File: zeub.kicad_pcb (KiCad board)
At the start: 2 copper layers, 177.8 x 60 mm, 377 parts, among them J1 debug-port, J2 OLED-128x32, J3 USB_C_Receptacle_USB2.0, J4 Barrel_Jack_Switch, J5 Conn_01x03, J6 Conn_01x03, Q1 AO3401A, Q2 AO3401A, Q3 AO3401A, Q4 AO3401A, Q5 AO3401A, SW1 SKRHA, SW2 RotaryEncoder_Switch, SW3 SW_Push, U1 IS31FL3729, U10 LTC4054ES5-4.2, U11 TMP117, U12 CMM4030D, U2 IS31FL3729, U3 IS31FL3729, U4 IS31FL3729, U5 holyiot-18010-no-underside, U6 MT25QL128ABA1ESE, U7 TLV1117-50, U8 XC6206PxxxMR, U9 SRV05-4

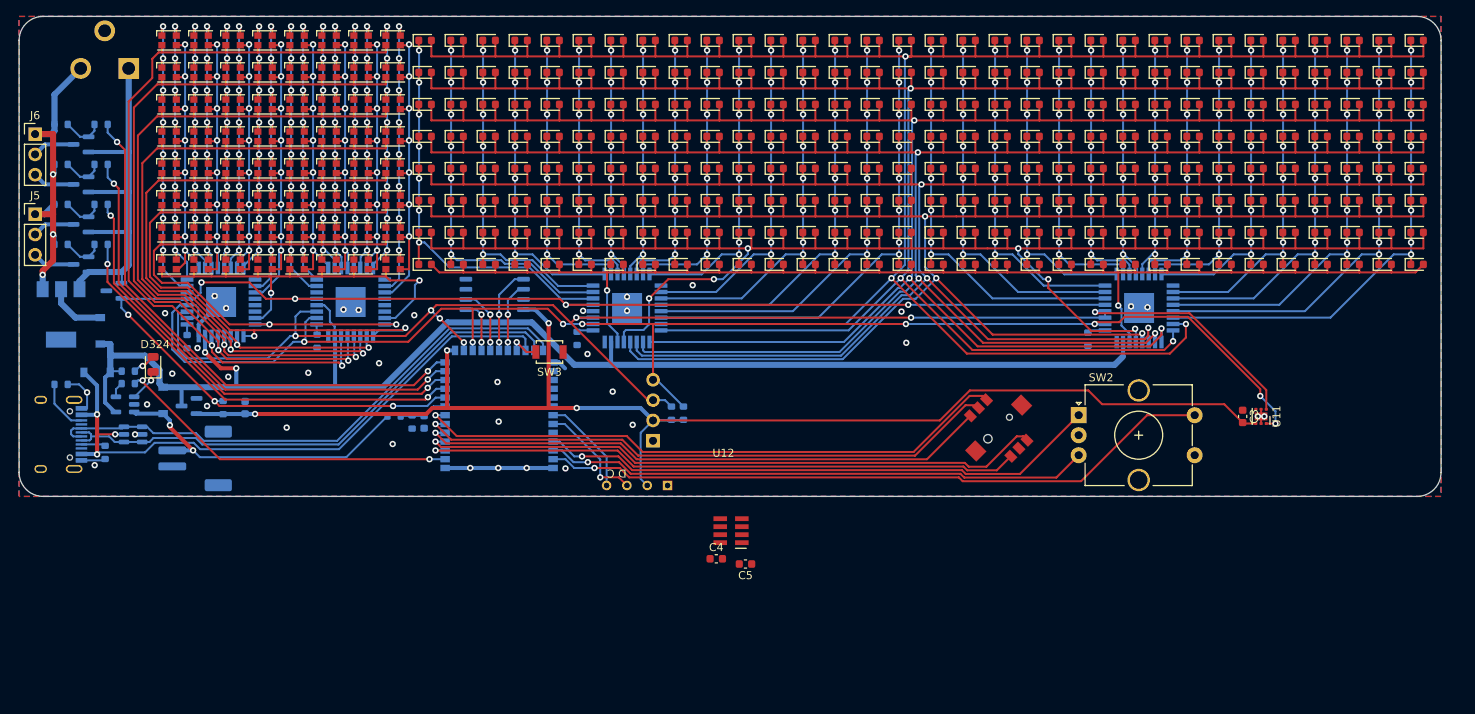
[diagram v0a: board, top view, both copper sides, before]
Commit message: Added audio stuff; rerouted for prep
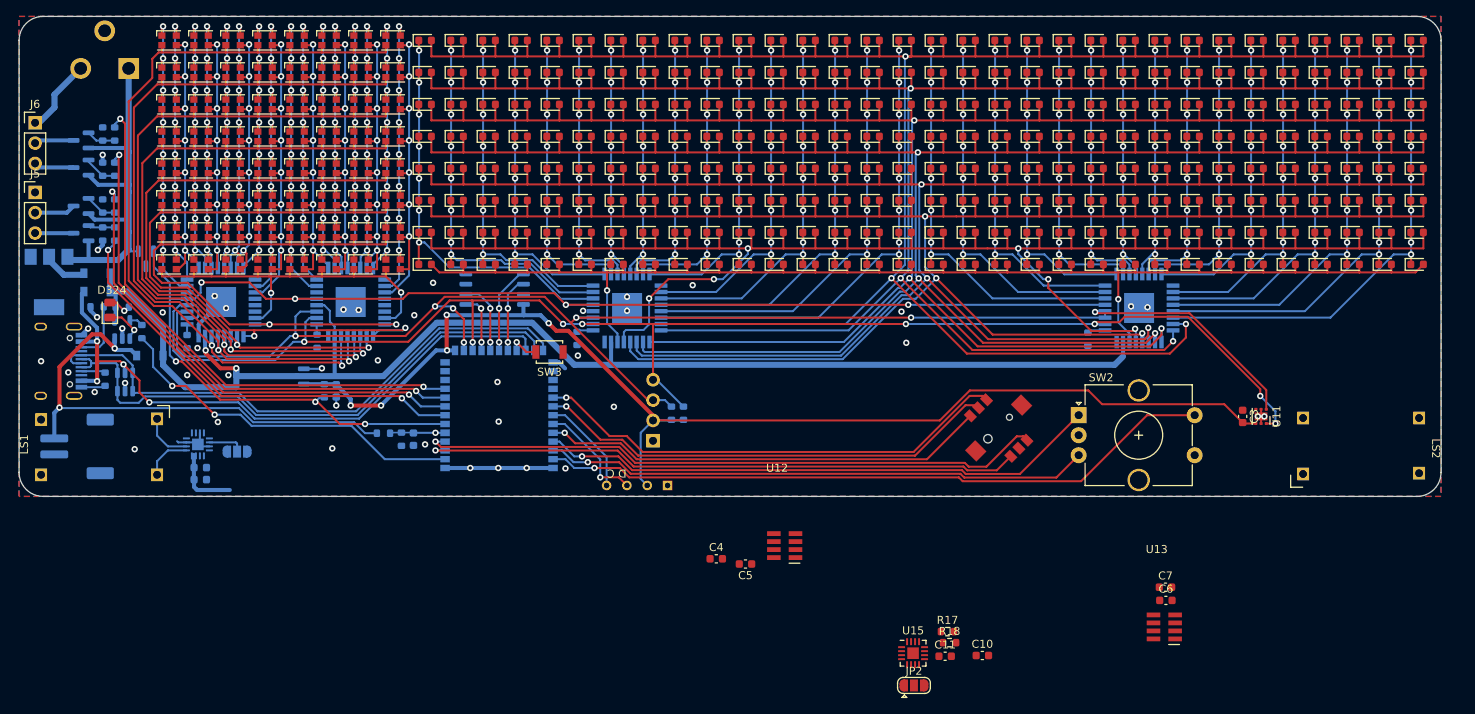
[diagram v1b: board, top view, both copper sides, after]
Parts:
- added C10: 0.1uF, Capacitor_SMD:C_0603_1608Metric, F.Cu at (101.7, 76.9)
- added C11: 10uF, Capacitor_SMD:C_0603_1608Metric, F.Cu at (97.0, 77.0)
- added C6: 10uF, Capacitor_SMD:C_0603_1608Metric, F.Cu at (124.6, 70.0)
- added C7: 0.1uF, Capacitor_SMD:C_0603_1608Metric, F.Cu at (124.5, 68.3)
- added C8: 0.1uF, Capacitor_SMD:C_0603_1608Metric, B.Cu at (3.90, 53.4)
- added C9: 10uF, Capacitor_SMD:C_0603_1608Metric, B.Cu at (3.90, 54.9)
- added JP1: SolderJumper_3_Open, Jumper:SolderJumper-3_P1.3mm_Open_RoundedPad1.0x1.5mm, B.Cu at (8.50, 51.4)
- added JP2: SolderJumper_3_Open, Jumper:SolderJumper-3_P1.3mm_Open_RoundedPad1.0x1.5mm, F.Cu at (93.1, 80.6)
- added LS1: Speaker, misc:CMS1609, F.Cu at (-8.75, 50.8)
- added LS2: Speaker, misc:CMS1609, F.Cu at (149.0, 50.8)
- added R17: 100k, Resistor_SMD:R_0603_1608Metric, F.Cu at (97.3, 73.9)
- added R18: 100k, Resistor_SMD:R_0603_1608Metric, F.Cu at (97.6, 75.3)
- added U13: CMM4030D, ic:CMM4030D_hand_solder, F.Cu at (124.4, 73.3)
- added U14: MAX98357A, Package_DFN_QFN:QFN-16-1EP_3x3mm_P0.5mm_EP1.45x1.45mm, B.Cu at (3.60, 50.5)
- added U15: MAX98357A, Package_DFN_QFN:QFN-16-1EP_3x3mm_P0.5mm_EP1.45x1.45mm, F.Cu at (93.0, 76.6)
- moved BT1 14.8 mm to (-11.5, 50.8)
- moved U8 13.9 mm to (15.9, 42.0)
- moved R73 12.8 mm to (19.4, 43.8), turned to -90 degrees
- moved C2 11.6 mm to (20.9, 43.8), turned to 90 degrees
- moved R10 10.7 mm to (-9.00, 33.3), turned to 0 degrees
- moved D321 10.1 mm to (-9.00, 31.4)
- moved U10 9.37 mm to (-5.85, 36.1), turned to 90 degrees
- moved J3 9.15 mm to (-15.0, 40.1)
- moved R9 9.15 mm to (-8.00, 42.4)
- moved D324 8.68 mm to (-7.40, 33.7)
- moved R11 8.05 mm to (-5.85, 33.3)
- moved D323 7.21 mm to (-9.00, 29.1), turned to 180 degrees
- moved U12 6.96 mm to (77.0, 63.1)
- moved R12 6.72 mm to (-3.40, 36.4), turned to -90 degrees
- moved U9 6.63 mm to (-5.50, 42.7), turned to 90 degrees
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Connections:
- U12 pad 2: unconnected-(U12-Pad2) -> (no net)
- U12 pad 3: unconnected-(U12-Pad3) -> LRCLK
- U12 pad 5: unconnected-(U12-Pad5) -> GND
- U12 pad 6: unconnected-(U12-Pad6) -> BCLK
- U12 pad 7: unconnected-(U12-Pad7) -> SDIN
- U5 pad 10: PWMY1 -> PWMW0
- U5 pad 11: PWMW1 -> unconnected-(U5-Pad11)
- U5 pad 12: PWMY0 -> unconnected-(U5-Pad12)
- U5 pad 13: PWMW0 -> unconnected-(U5-Pad13)
- U5 pad 36: unconnected-(U5-Pad36) -> C
- U5 pad 39: unconnected-(U5-Pad39) -> E
- U5 pad 40: unconnected-(U5-Pad40) -> A
- U5 pad 5: C -> BAT_MEAS
- U5 pad 6: E -> HAS_12V
- U5 pad 7: A -> PWMY1
- U5 pad 8: BAT_MEAS -> PWMW1
- U5 pad 9: HAS_12V -> PWMY0
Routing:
- net +BATT: track 39.2 -> 63.9 mm
- net GND: track 73.0 -> 50.8 mm, vias 40 -> 44
- net C: track 71.7 -> 55.8 mm
- net E: track 73.5 -> 58.5 mm
- net A: track 75.1 -> 60.1 mm
- net +3V3: track 172.2 -> 161.0 mm, vias 4 -> 5
- net +5V: track 180.9 -> 171.1 mm
- net Net-(U14-Pad10): track 0.00 -> 6.32 mm
- net Net-(LS1-Pad2): track 0.00 -> 5.92 mm
- net Net-(JP1-Pad2): track 0.00 -> 4.53 mm
- net /led/RGB_C7: track 53.7 -> 49.6 mm
- net +12V: track 49.0 -> 52.6 mm
- net D-: track 66.8 -> 70.3 mm
- net D+: track 69.3 -> 71.7 mm
- net PWMW1: track 58.0 -> 60.4 mm
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
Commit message: fully routed
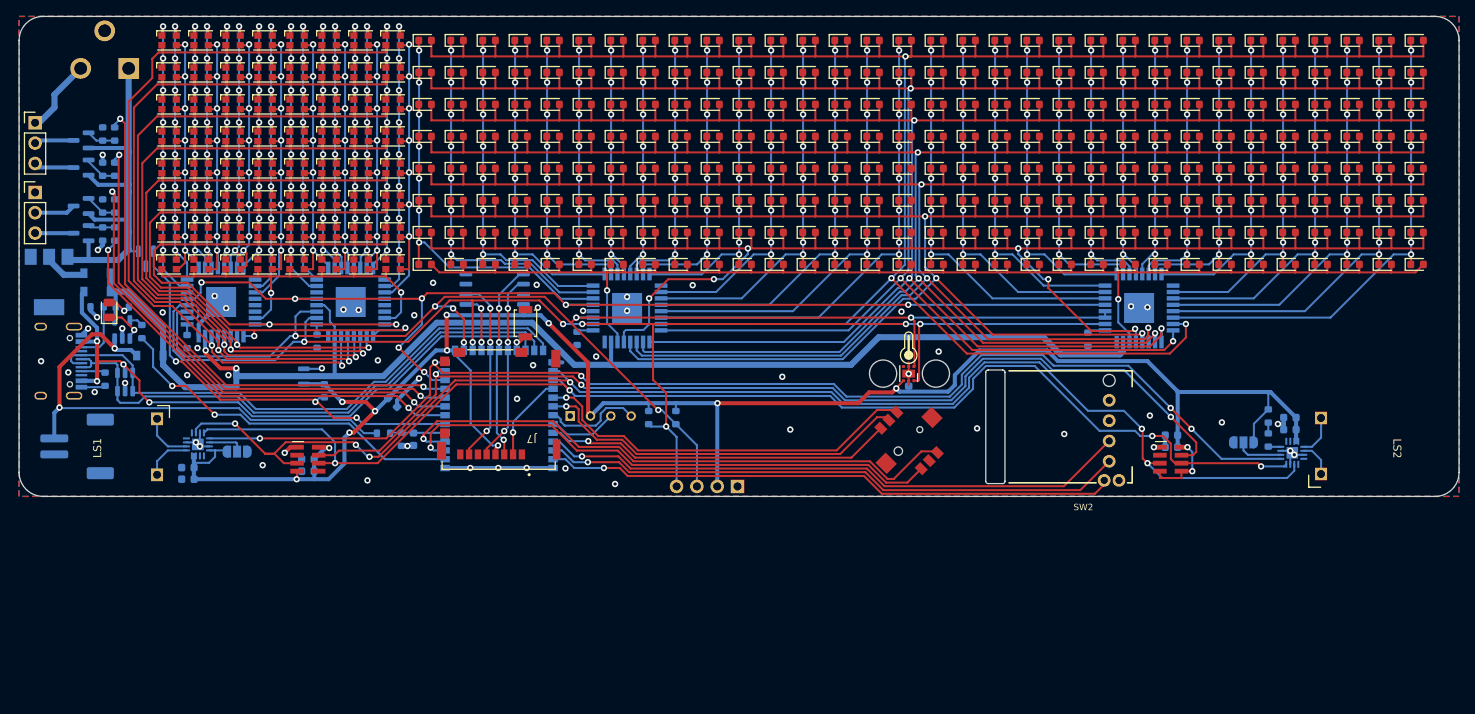
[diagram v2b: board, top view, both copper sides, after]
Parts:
- added J7: Micro_SD_Card_Det, misc:molex-503182-1852, F.Cu at (40.2, 45.3)
- C10, C11, C3, C4, C5, C6, C7, J1, JP2, R17, R18, U15: moved to B.Cu
- J2: footprint display:OLED-128x32-cutout -> display:OLED-128x64
- SW2: footprint Rotary_Encoder:RotaryEncoder_Alps_EC12E-Switch_Vertical_H20mm_CircularMountingHoles -> switch:EVQWGD001
- moved U12 60.6 mm to (17.4, 52.4), turned to 180 degrees
- moved C5 56.2 mm to (17.4, 52.4), turned to 0 degrees
- moved U15 53.6 mm to (140.4, 51.5)
- moved C11 52.4 mm to (140.1, 47.1)
- moved C4 52.2 mm to (17.4, 53.9)
- moved JP2 51.2 mm to (134.3, 50.2)
- moved R18 48.9 mm to (137.4, 47.0), turned to 90 degrees
- moved C10 47.7 mm to (140.1, 48.6)
- moved R17 46.7 mm to (137.4, 50.0), turned to 90 degrees
- moved U11 44.4 mm to (92.5, 41.6)
- moved C3 42.0 mm to (92.5, 42.5)
- moved U13 21.0 mm to (125.2, 52.4), turned to 180 degrees
- moved C6 20.7 mm to (125.3, 49.4)
- moved J2 17.6 mm to (67.2, 55.8), turned to 180 degrees
- moved C7 17.5 mm to (125.3, 50.9)
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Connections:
- LS2 pad 1: Net-(LS2-Pad1) -> Net-(U15-Pad10)
- LS2 pad 2: Net-(LS2-Pad2) -> Net-(U15-Pad9)
- SW2 pad S1: ENC_PUSH -> GND
- SW2 pad S2: GND -> ENC_PUSH
- U1 pad 29: HAS_12V -> ~{LED_SHDN}
- U15 pad 10: Net-(LS2-Pad2) -> Net-(U15-Pad10)
- U15 pad 9: Net-(LS2-Pad1) -> Net-(U15-Pad9)
- U2 pad 29: HAS_12V -> ~{LED_SHDN}
- U3 pad 29: HAS_12V -> ~{LED_SHDN}
- U4 pad 29: HAS_12V -> ~{LED_SHDN}
- U5 pad 11: unconnected-(U5-Pad11) -> ~{LED_SHDN}
- U5 pad 12: unconnected-(U5-Pad12) -> SDIN
- U5 pad 13: unconnected-(U5-Pad13) -> SDOUT
- U5 pad 34: ENC_B -> ENC_A
- U5 pad 35: ENC_A -> ENC_B
- U5 pad 41: unconnected-(U5-Pad41) -> SD_CS
- U5 pad 42: unconnected-(U5-Pad42) -> BCLK
- U5 pad 43: unconnected-(U5-Pad43) -> LRCLK
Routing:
- net LRCLK: track 0.00 -> 166.9 mm, vias 0 -> 6
- net BCLK: track 0.00 -> 158.0 mm, vias 0 -> 4
- net SDOUT: track 0.00 -> 151.3 mm, vias 0 -> 5
- net ~{LED_SHDN}: track 0.00 -> 139.0 mm, vias 0 -> 7
- net SDIN: track 0.00 -> 128.5 mm, vias 0 -> 3
- net HAS_12V: track 179.7 -> 53.4 mm, vias 7 -> 3
- net +3V3: track 161.0 -> 254.2 mm, vias 5 -> 13
- net MISO: track 9.24 -> 23.3 mm, vias 2 -> 3
- net ENC_PUSH: track 84.8 -> 71.2 mm
- net SCK: track 9.48 -> 22.9 mm, vias 2 -> 3
- net MOSI: track 11.1 -> 24.1 mm, vias 2 -> 3
- net GND: track 50.8 -> 63.5 mm, vias 44 -> 57
- net SCL: track 189.4 -> 176.9 mm
- net C: track 55.8 -> 43.8 mm
- net SDA: track 199.8 -> 188.2 mm, vias 8 -> 7
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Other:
- board size 177.8 x 60 mm -> 180 x 60 mm

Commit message: first version
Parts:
- added Q6: AO3401A, Package_TO_SOT_SMD:SOT-23, B.Cu at (-13.6, 10.7)
- added Q7: AO3401A, Package_TO_SOT_SMD:SOT-23, B.Cu at (-13.6, 14.6)
- added Q8: AO3401A, Package_TO_SOT_SMD:SOT-23, B.Cu at (-13.6, 19.4)
- added Q9: AO3401A, Package_TO_SOT_SMD:SOT-23, B.Cu at (-13.7, 23.7)
- added R19: 10k, Resistor_SMD:R_0603_1608Metric, B.Cu at (-10.9, 14.8)
- added R20: 10k, Resistor_SMD:R_0603_1608Metric, B.Cu at (-10.9, 19.6)
- added R21: 10k, Resistor_SMD:R_0603_1608Metric, B.Cu at (-11.0, 23.7)
- added R22: 100k, Resistor_SMD:R_0603_1608Metric, B.Cu at (-5.50, 10.5)
- added REF**: jlc-tooling-hole, misc:jlc-tooling-hole, F.Cu at (151.2, 50.8)
- added REF**: jlc-tooling-hole, misc:jlc-tooling-hole, F.Cu at (-14.6, 0.50)
- added REF**: jlc-tooling-hole, misc:jlc-tooling-hole, F.Cu at (-8.75, 50.8)
- D257, D258, D259, D260, D261, D262, D263, D264, D265, D266, D267, D268, D269, D270, D271, D272, D273, D274, D275, D276, D277, D278, D279, D280, D281, D282, D283, D284, D285, D286, D287, D288, D289, D290, D291, D292, D293, D294, D295, D296, D297, D298, D299, D300, D301, D302, D303, D304, D305, D306, D307, D308, D309, D310, D311, D312, D313, D314, D315, D316, D317, D318, D319, D320: value LED_RABG -> LED_BGRA
- Q1, Q2, Q3, Q4, Q5: value AO3401A -> AO3400A
- R5: value 100k -> 10k
- moved Q1 3.33 mm to (-8.20, 10.7)
- moved R7 3.18 mm to (-5.50, 19.2), turned to -90 degrees
- moved R3 3.18 mm to (-4.00, 19.2), turned to 90 degrees
- moved R6 3.13 mm to (-5.50, 14.7), turned to -90 degrees
- moved R2 3.13 mm to (-4.00, 14.7), turned to 90 degrees
- moved Q3 3.09 mm to (-8.20, 19.4)
- moved R1 3.05 mm to (-4.00, 10.5), turned to 90 degrees
- moved Q2 2.97 mm to (-8.20, 14.9)
- moved R5 2.82 mm to (-10.9, 10.6)
- moved R8 2.73 mm to (-5.60, 23.8)
- moved R4 2.73 mm to (-4.10, 23.8)
- moved Q4 2.71 mm to (-8.30, 23.9)
- moved C3 0.87 mm to (92.0, 41.7)
- moved U11 0.45 mm to (92.0, 41.6)
- moved D323 0.10 mm to (-9.00, 29.0)
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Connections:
- D257 pad 1: /led/RGB_R0 -> /led/RGB_B0
- D257 pad 2: /led/RGB_C0 -> /led/RGB_G0
- D257 pad 3: /led/RGB_B0 -> /led/RGB_R0
- D257 pad 4: /led/RGB_G0 -> /led/RGB_C0
- D258 pad 1: /led/RGB_R0 -> /led/RGB_B0
- D258 pad 2: /led/RGB_C1 -> /led/RGB_G0
- D258 pad 3: /led/RGB_B0 -> /led/RGB_R0
- D258 pad 4: /led/RGB_G0 -> /led/RGB_C1
- D259 pad 1: /led/RGB_R0 -> /led/RGB_B0
- D259 pad 2: /led/RGB_C2 -> /led/RGB_G0
- D259 pad 3: /led/RGB_B0 -> /led/RGB_R0
- D259 pad 4: /led/RGB_G0 -> /led/RGB_C2
- D260 pad 1: /led/RGB_R0 -> /led/RGB_B0
- D260 pad 2: /led/RGB_C3 -> /led/RGB_G0
- D260 pad 3: /led/RGB_B0 -> /led/RGB_R0
- D260 pad 4: /led/RGB_G0 -> /led/RGB_C3
- D261 pad 1: /led/RGB_R0 -> /led/RGB_B0
- D261 pad 2: /led/RGB_C4 -> /led/RGB_G0
- D261 pad 3: /led/RGB_B0 -> /led/RGB_R0
- D261 pad 4: /led/RGB_G0 -> /led/RGB_C4
- D262 pad 1: /led/RGB_R0 -> /led/RGB_B0
- D262 pad 2: /led/RGB_C5 -> /led/RGB_G0
- D262 pad 3: /led/RGB_B0 -> /led/RGB_R0
- D262 pad 4: /led/RGB_G0 -> /led/RGB_C5
- D263 pad 1: /led/RGB_R0 -> /led/RGB_B0
- D263 pad 2: /led/RGB_C6 -> /led/RGB_G0
- D263 pad 3: /led/RGB_B0 -> /led/RGB_R0
- D263 pad 4: /led/RGB_G0 -> /led/RGB_C6
- D264 pad 1: /led/RGB_R0 -> /led/RGB_B0
- D264 pad 2: /led/RGB_C7 -> /led/RGB_G0
- D264 pad 3: /led/RGB_B0 -> /led/RGB_R0
- D264 pad 4: /led/RGB_G0 -> /led/RGB_C7
- D265 pad 1: /led/RGB_R1 -> /led/RGB_B1
- D265 pad 2: /led/RGB_C0 -> /led/RGB_G1
- D265 pad 3: /led/RGB_B1 -> /led/RGB_R1
- D265 pad 4: /led/RGB_G1 -> /led/RGB_C0
- D266 pad 1: /led/RGB_R1 -> /led/RGB_B1
- D266 pad 2: /led/RGB_C1 -> /led/RGB_G1
- D266 pad 3: /led/RGB_B1 -> /led/RGB_R1
- D266 pad 4: /led/RGB_G1 -> /led/RGB_C1
- D267 pad 1: /led/RGB_R1 -> /led/RGB_B1
- D267 pad 2: /led/RGB_C2 -> /led/RGB_G1
- D267 pad 3: /led/RGB_B1 -> /led/RGB_R1
- D267 pad 4: /led/RGB_G1 -> /led/RGB_C2
- D268 pad 1: /led/RGB_R1 -> /led/RGB_B1
- D268 pad 2: /led/RGB_C3 -> /led/RGB_G1
- D268 pad 3: /led/RGB_B1 -> /led/RGB_R1
- D268 pad 4: /led/RGB_G1 -> /led/RGB_C3
- D269 pad 1: /led/RGB_R1 -> /led/RGB_B1
- D269 pad 2: /led/RGB_C4 -> /led/RGB_G1
- D269 pad 3: /led/RGB_B1 -> /led/RGB_R1
- D269 pad 4: /led/RGB_G1 -> /led/RGB_C4
- D270 pad 1: /led/RGB_R1 -> /led/RGB_B1
- D270 pad 2: /led/RGB_C5 -> /led/RGB_G1
- D270 pad 3: /led/RGB_B1 -> /led/RGB_R1
- D270 pad 4: /led/RGB_G1 -> /led/RGB_C5
- D271 pad 1: /led/RGB_R1 -> /led/RGB_B1
- D271 pad 2: /led/RGB_C6 -> /led/RGB_G1
- D271 pad 3: /led/RGB_B1 -> /led/RGB_R1
- D271 pad 4: /led/RGB_G1 -> /led/RGB_C6
- D272 pad 1: /led/RGB_R1 -> /led/RGB_B1
- D272 pad 2: /led/RGB_C7 -> /led/RGB_G1
- D272 pad 3: /led/RGB_B1 -> /led/RGB_R1
- D272 pad 4: /led/RGB_G1 -> /led/RGB_C7
- D273 pad 1: /led/RGB_R2 -> /led/RGB_B2
- D273 pad 2: /led/RGB_C0 -> /led/RGB_G2
- D273 pad 3: /led/RGB_B2 -> /led/RGB_R2
- D273 pad 4: /led/RGB_G2 -> /led/RGB_C0
- D274 pad 1: /led/RGB_R2 -> /led/RGB_B2
- D274 pad 2: /led/RGB_C1 -> /led/RGB_G2
- D274 pad 3: /led/RGB_B2 -> /led/RGB_R2
- D274 pad 4: /led/RGB_G2 -> /led/RGB_C1
- D275 pad 1: /led/RGB_R2 -> /led/RGB_B2
- D275 pad 2: /led/RGB_C2 -> /led/RGB_G2
- D275 pad 3: /led/RGB_B2 -> /led/RGB_R2
- D275 pad 4: /led/RGB_G2 -> /led/RGB_C2
- D276 pad 1: /led/RGB_R2 -> /led/RGB_B2
- D276 pad 2: /led/RGB_C3 -> /led/RGB_G2
- D276 pad 3: /led/RGB_B2 -> /led/RGB_R2
- D276 pad 4: /led/RGB_G2 -> /led/RGB_C3
- D277 pad 1: /led/RGB_R2 -> /led/RGB_B2
- D277 pad 2: /led/RGB_C4 -> /led/RGB_G2
- D277 pad 3: /led/RGB_B2 -> /led/RGB_R2
- D277 pad 4: /led/RGB_G2 -> /led/RGB_C4
- D278 pad 1: /led/RGB_R2 -> /led/RGB_B2
- D278 pad 2: /led/RGB_C5 -> /led/RGB_G2
- D278 pad 3: /led/RGB_B2 -> /led/RGB_R2
- D278 pad 4: /led/RGB_G2 -> /led/RGB_C5
- D279 pad 1: /led/RGB_R2 -> /led/RGB_B2
- D279 pad 2: /led/RGB_C6 -> /led/RGB_G2
- D279 pad 3: /led/RGB_B2 -> /led/RGB_R2
- D279 pad 4: /led/RGB_G2 -> /led/RGB_C6
- D280 pad 1: /led/RGB_R2 -> /led/RGB_B2
- D280 pad 2: /led/RGB_C7 -> /led/RGB_G2
- D280 pad 3: /led/RGB_B2 -> /led/RGB_R2
- D280 pad 4: /led/RGB_G2 -> /led/RGB_C7
- D281 pad 1: /led/RGB_R3 -> /led/RGB_B3
- D281 pad 2: /led/RGB_C0 -> /led/RGB_G3
- D281 pad 3: /led/RGB_B3 -> /led/RGB_R3
- D281 pad 4: /led/RGB_G3 -> /led/RGB_C0
- D282 pad 1: /led/RGB_R3 -> /led/RGB_B3
- D282 pad 2: /led/RGB_C1 -> /led/RGB_G3
- D282 pad 3: /led/RGB_B3 -> /led/RGB_R3
- D282 pad 4: /led/RGB_G3 -> /led/RGB_C1
- D283 pad 1: /led/RGB_R3 -> /led/RGB_B3
- D283 pad 2: /led/RGB_C2 -> /led/RGB_G3
- D283 pad 3: /led/RGB_B3 -> /led/RGB_R3
- D283 pad 4: /led/RGB_G3 -> /led/RGB_C2
- D284 pad 1: /led/RGB_R3 -> /led/RGB_B3
- D284 pad 2: /led/RGB_C3 -> /led/RGB_G3
- D284 pad 3: /led/RGB_B3 -> /led/RGB_R3
- D284 pad 4: /led/RGB_G3 -> /led/RGB_C3
- D285 pad 1: /led/RGB_R3 -> /led/RGB_B3
- D285 pad 2: /led/RGB_C4 -> /led/RGB_G3
- D285 pad 3: /led/RGB_B3 -> /led/RGB_R3
- D285 pad 4: /led/RGB_G3 -> /led/RGB_C4
- D286 pad 1: /led/RGB_R3 -> /led/RGB_B3
- D286 pad 2: /led/RGB_C5 -> /led/RGB_G3
- D286 pad 3: /led/RGB_B3 -> /led/RGB_R3
- D286 pad 4: /led/RGB_G3 -> /led/RGB_C5
- D287 pad 1: /led/RGB_R3 -> /led/RGB_B3
- D287 pad 2: /led/RGB_C6 -> /led/RGB_G3
- D287 pad 3: /led/RGB_B3 -> /led/RGB_R3
- D287 pad 4: /led/RGB_G3 -> /led/RGB_C6
- D288 pad 1: /led/RGB_R3 -> /led/RGB_B3
- D288 pad 2: /led/RGB_C7 -> /led/RGB_G3
- D288 pad 3: /led/RGB_B3 -> /led/RGB_R3
- D288 pad 4: /led/RGB_G3 -> /led/RGB_C7
- D289 pad 1: /led/RGB_R4 -> /led/RGB_B4
- D289 pad 2: /led/RGB_C0 -> /led/RGB_G4
- D289 pad 3: /led/RGB_B4 -> /led/RGB_R4
- D289 pad 4: /led/RGB_G4 -> /led/RGB_C0
- D290 pad 1: /led/RGB_R4 -> /led/RGB_B4
- D290 pad 2: /led/RGB_C1 -> /led/RGB_G4
- D290 pad 3: /led/RGB_B4 -> /led/RGB_R4
- D290 pad 4: /led/RGB_G4 -> /led/RGB_C1
- D291 pad 1: /led/RGB_R4 -> /led/RGB_B4
- D291 pad 2: /led/RGB_C2 -> /led/RGB_G4
- D291 pad 3: /led/RGB_B4 -> /led/RGB_R4
- D291 pad 4: /led/RGB_G4 -> /led/RGB_C2
- D292 pad 1: /led/RGB_R4 -> /led/RGB_B4
- D292 pad 2: /led/RGB_C3 -> /led/RGB_G4
- D292 pad 3: /led/RGB_B4 -> /led/RGB_R4
- D292 pad 4: /led/RGB_G4 -> /led/RGB_C3
- D293 pad 1: /led/RGB_R4 -> /led/RGB_B4
- D293 pad 2: /led/RGB_C4 -> /led/RGB_G4
- D293 pad 3: /led/RGB_B4 -> /led/RGB_R4
- D293 pad 4: /led/RGB_G4 -> /led/RGB_C4
- D294 pad 1: /led/RGB_R4 -> /led/RGB_B4
- D294 pad 2: /led/RGB_C5 -> /led/RGB_G4
- D294 pad 3: /led/RGB_B4 -> /led/RGB_R4
- D294 pad 4: /led/RGB_G4 -> /led/RGB_C5
- D295 pad 1: /led/RGB_R4 -> /led/RGB_B4
- D295 pad 2: /led/RGB_C6 -> /led/RGB_G4
- D295 pad 3: /led/RGB_B4 -> /led/RGB_R4
- D295 pad 4: /led/RGB_G4 -> /led/RGB_C6
- D296 pad 1: /led/RGB_R4 -> /led/RGB_B4
- D296 pad 2: /led/RGB_C7 -> /led/RGB_G4
- D296 pad 3: /led/RGB_B4 -> /led/RGB_R4
- D296 pad 4: /led/RGB_G4 -> /led/RGB_C7
- D297 pad 1: /led/RGB_R5 -> /led/RGB_B5
- D297 pad 2: /led/RGB_C0 -> /led/RGB_G5
- D297 pad 3: /led/RGB_B5 -> /led/RGB_R5
- D297 pad 4: /led/RGB_G5 -> /led/RGB_C0
- D298 pad 1: /led/RGB_R5 -> /led/RGB_B5
- D298 pad 2: /led/RGB_C1 -> /led/RGB_G5
- D298 pad 3: /led/RGB_B5 -> /led/RGB_R5
- D298 pad 4: /led/RGB_G5 -> /led/RGB_C1
- D299 pad 1: /led/RGB_R5 -> /led/RGB_B5
- D299 pad 2: /led/RGB_C2 -> /led/RGB_G5
- D299 pad 3: /led/RGB_B5 -> /led/RGB_R5
- D299 pad 4: /led/RGB_G5 -> /led/RGB_C2
- D300 pad 1: /led/RGB_R5 -> /led/RGB_B5
- D300 pad 2: /led/RGB_C3 -> /led/RGB_G5
- D300 pad 3: /led/RGB_B5 -> /led/RGB_R5
- D300 pad 4: /led/RGB_G5 -> /led/RGB_C3
- D301 pad 1: /led/RGB_R5 -> /led/RGB_B5
- D301 pad 2: /led/RGB_C4 -> /led/RGB_G5
- D301 pad 3: /led/RGB_B5 -> /led/RGB_R5
- D301 pad 4: /led/RGB_G5 -> /led/RGB_C4
- D302 pad 1: /led/RGB_R5 -> /led/RGB_B5
- D302 pad 2: /led/RGB_C5 -> /led/RGB_G5
- D302 pad 3: /led/RGB_B5 -> /led/RGB_R5
- D302 pad 4: /led/RGB_G5 -> /led/RGB_C5
- D303 pad 1: /led/RGB_R5 -> /led/RGB_B5
- D303 pad 2: /led/RGB_C6 -> /led/RGB_G5
- D303 pad 3: /led/RGB_B5 -> /led/RGB_R5
- D303 pad 4: /led/RGB_G5 -> /led/RGB_C6
- D304 pad 1: /led/RGB_R5 -> /led/RGB_B5
- D304 pad 2: /led/RGB_C7 -> /led/RGB_G5
- D304 pad 3: /led/RGB_B5 -> /led/RGB_R5
- D304 pad 4: /led/RGB_G5 -> /led/RGB_C7
- D305 pad 1: /led/RGB_R6 -> /led/RGB_B6
- D305 pad 2: /led/RGB_C0 -> /led/RGB_G6
- D305 pad 3: /led/RGB_B6 -> /led/RGB_R6
- D305 pad 4: /led/RGB_G6 -> /led/RGB_C0
- D306 pad 1: /led/RGB_R6 -> /led/RGB_B6
- D306 pad 2: /led/RGB_C1 -> /led/RGB_G6
- D306 pad 3: /led/RGB_B6 -> /led/RGB_R6
- D306 pad 4: /led/RGB_G6 -> /led/RGB_C1
- D307 pad 1: /led/RGB_R6 -> /led/RGB_B6
- D307 pad 2: /led/RGB_C2 -> /led/RGB_G6
- D307 pad 3: /led/RGB_B6 -> /led/RGB_R6
- D307 pad 4: /led/RGB_G6 -> /led/RGB_C2
- D308 pad 1: /led/RGB_R6 -> /led/RGB_B6
- D308 pad 2: /led/RGB_C3 -> /led/RGB_G6
- D308 pad 3: /led/RGB_B6 -> /led/RGB_R6
- D308 pad 4: /led/RGB_G6 -> /led/RGB_C3
- D309 pad 1: /led/RGB_R6 -> /led/RGB_B6
- D309 pad 2: /led/RGB_C4 -> /led/RGB_G6
- D309 pad 3: /led/RGB_B6 -> /led/RGB_R6
- D309 pad 4: /led/RGB_G6 -> /led/RGB_C4
- D310 pad 1: /led/RGB_R6 -> /led/RGB_B6
- D310 pad 2: /led/RGB_C5 -> /led/RGB_G6
- D310 pad 3: /led/RGB_B6 -> /led/RGB_R6
- D310 pad 4: /led/RGB_G6 -> /led/RGB_C5
- D311 pad 1: /led/RGB_R6 -> /led/RGB_B6
- D311 pad 2: /led/RGB_C6 -> /led/RGB_G6
- D311 pad 3: /led/RGB_B6 -> /led/RGB_R6
- D311 pad 4: /led/RGB_G6 -> /led/RGB_C6
- D312 pad 1: /led/RGB_R6 -> /led/RGB_B6
- D312 pad 2: /led/RGB_C7 -> /led/RGB_G6
- D312 pad 3: /led/RGB_B6 -> /led/RGB_R6
- D312 pad 4: /led/RGB_G6 -> /led/RGB_C7
- D313 pad 1: /led/RGB_R7 -> /led/RGB_B7
- D313 pad 2: /led/RGB_C0 -> /led/RGB_G7
- D313 pad 3: /led/RGB_B7 -> /led/RGB_R7
- D313 pad 4: /led/RGB_G7 -> /led/RGB_C0
- D314 pad 1: /led/RGB_R7 -> /led/RGB_B7
- D314 pad 2: /led/RGB_C1 -> /led/RGB_G7
- D314 pad 3: /led/RGB_B7 -> /led/RGB_R7
- D314 pad 4: /led/RGB_G7 -> /led/RGB_C1
- D315 pad 1: /led/RGB_R7 -> /led/RGB_B7
- D315 pad 2: /led/RGB_C2 -> /led/RGB_G7
- D315 pad 3: /led/RGB_B7 -> /led/RGB_R7
- D315 pad 4: /led/RGB_G7 -> /led/RGB_C2
- D316 pad 1: /led/RGB_R7 -> /led/RGB_B7
- D316 pad 2: /led/RGB_C3 -> /led/RGB_G7
- D316 pad 3: /led/RGB_B7 -> /led/RGB_R7
- D316 pad 4: /led/RGB_G7 -> /led/RGB_C3
- D317 pad 1: /led/RGB_R7 -> /led/RGB_B7
- D317 pad 2: /led/RGB_C4 -> /led/RGB_G7
- D317 pad 3: /led/RGB_B7 -> /led/RGB_R7
- D317 pad 4: /led/RGB_G7 -> /led/RGB_C4
- D318 pad 1: /led/RGB_R7 -> /led/RGB_B7
- D318 pad 2: /led/RGB_C5 -> /led/RGB_G7
- D318 pad 3: /led/RGB_B7 -> /led/RGB_R7
- D318 pad 4: /led/RGB_G7 -> /led/RGB_C5
- D319 pad 1: /led/RGB_R7 -> /led/RGB_B7
- D319 pad 2: /led/RGB_C6 -> /led/RGB_G7
- D319 pad 3: /led/RGB_B7 -> /led/RGB_R7
- D319 pad 4: /led/RGB_G7 -> /led/RGB_C6
- D320 pad 1: /led/RGB_R7 -> /led/RGB_B7
- D320 pad 2: /led/RGB_C7 -> /led/RGB_G7
- D320 pad 3: /led/RGB_B7 -> /led/RGB_R7
- D320 pad 4: /led/RGB_G7 -> /led/RGB_C7
- Q1 pad 2: +12V -> GND
- Q1 pad 3: LEDW0 -> Net-(Q1-Pad3)
- Q2 pad 2: +12V -> GND
- Q2 pad 3: LEDY0 -> Net-(Q2-Pad3)
- Q3 pad 2: +12V -> GND
- Q3 pad 3: LEDW1 -> Net-(Q3-Pad3)
- Q4 pad 2: +12V -> GND
- Q4 pad 3: LEDY1 -> Net-(Q4-Pad3)
- Q5 pad 2: HAS_12V -> GND
- Q5 pad 3: GND -> HAS_12V
- R5 pad 1: Net-(Q1-Pad1) -> +12V
- R5 pad 2: GND -> Net-(Q1-Pad3)
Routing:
- net +12V: track 52.6 -> 69.8 mm
- net Net-(Q2-Pad3): track 0.00 -> 4.04 mm
- net Net-(Q4-Pad3): track 0.00 -> 4.00 mm
- net Net-(Q3-Pad3): track 0.00 -> 3.92 mm
- net Net-(Q1-Pad3): track 0.00 -> 3.92 mm
- net PWMY1: track 54.6 -> 57.2 mm
- net PWMW0: track 67.7 -> 65.1 mm
- net LEDY1: track 4.79 -> 2.27 mm
- net LEDY0: track 5.00 -> 2.54 mm
- net GND: track 63.5 -> 65.9 mm, vias 57 -> 59
- net PWMY0: track 64.0 -> 62.0 mm
- net LEDW1: track 5.16 -> 3.47 mm
- net LEDW0: track 4.47 -> 3.10 mm
- net +3V3: track 254.2 -> 255.5 mm
- net Net-(Q2-Pad1): track 4.21 -> 3.29 mm
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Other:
- outline, holes or cut-outs redrawn
- board text added: "JLCJLCJLCJLC"
